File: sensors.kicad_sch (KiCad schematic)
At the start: 12 parts, among them U2 BMI088, U3 MMC5983MA, U4 MS5607-02BA

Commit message: rs232,can,ind,storage,usb v01
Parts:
- renumbered C34 to C27, C33 to C28, C25 to C29, C22 to C30, C21 to C31, C24 to C32, C23 to C33, C35 to C34, C20 to C35, U3 to U2, U2 to U3
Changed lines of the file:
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@@
 		(dnp no)
 		(fields_autoplaced yes)
-		(property "Reference" "#PWR013"
+		(property "Reference" "#PWR023"
 			(at 52.07 68.58 0)
 			(effects
@@
 			(project "hoppen_fc"
 				(path "/abe950a1-9eef-4508-9fd4-31d3e723e029/c85454e5-a89e-41eb-a5ed-71b4fc4cf13a/328607b5-eaf8-4cbb-82fe-138ea1b53a88"
-					(reference "#PWR013")
+					(reference "#PWR023")
 					(unit 1)
 				)
@@
 		(dnp no)
 		(fields_autoplaced yes)
-		(property "Reference" "#PWR012"
+		(property "Reference" "#PWR027"
 			(at 96.52 68.58 0)
 			(effects
@@
 			(project "hoppen_fc"
 				(path "/abe950a1-9eef-4508-9fd4-31d3e723e029/c85454e5-a89e-41eb-a5ed-71b4fc4cf13a/328607b5-eaf8-4cbb-82fe-138ea1b53a88"
-					(reference "#PWR012")
+					(reference "#PWR027")
 					(unit 1)
 				)
@@
 		(dnp no)
 		(fields_autoplaced yes)
-		(property "Reference" "#PWR019"
+		(property "Reference" "#PWR025"
 			(at 85.09 187.96 0)
 			(effects
@@
 			(project "hoppen_fc"
 				(path "/abe950a1-9eef-4508-9fd4-31d3e723e029/c85454e5-a89e-41eb-a5ed-71b4fc4cf13a/328607b5-eaf8-4cbb-82fe-138ea1b53a88"
-					(reference "#PWR019")
+					(reference "#PWR025")
 					(unit 1)
 				)
@@
 		(dnp no)
 		(fields_autoplaced yes)
-		(property "Reference" "#PWR017"
+		(property "Reference" "#PWR028"
 			(at 96.52 114.3 0)
 			(effects
@@
 			(project "hoppen_fc"
 				(path "/abe950a1-9eef-4508-9fd4-31d3e723e029/c85454e5-a89e-41eb-a5ed-71b4fc4cf13a/328607b5-eaf8-4cbb-82fe-138ea1b53a88"
-					(reference "#PWR017")
+					(reference "#PWR028")
 					(unit 1)
 				)
@@
 		(dnp no)
 		(fields_autoplaced yes)
-		(property "Reference" "#PWR020"
+		(property "Reference" "#PWR030"
 			(at 99.06 154.94 0)
 			(effects
@@
 			(project "hoppen_fc"
 				(path "/abe950a1-9eef-4508-9fd4-31d3e723e029/c85454e5-a89e-41eb-a5ed-71b4fc4cf13a/328607b5-eaf8-4cbb-82fe-138ea1b53a88"
-					(reference "#PWR020")
+					(reference "#PWR030")
 					(unit 1)
 				)
@@
 		(dnp no)
 		(fields_autoplaced yes)
-		(property "Reference" "C34"
+		(property "Reference" "C27"
 			(at 46.99 143.5099 0)
 			(effects
@@
 			(project "hoppen_fc"
 				(path "/abe950a1-9eef-4508-9fd4-31d3e723e029/c85454e5-a89e-41eb-a5ed-71b4fc4cf13a/328607b5-eaf8-4cbb-82fe-138ea1b53a88"
-					(reference "C34")
+					(reference "C27")
 					(unit 1)
 				)
@@
 		(dnp no)
 		(fields_autoplaced yes)
-		(property "Reference" "C23"
+		(property "Reference" "C33"
 			(at 102.87 172.7199 0)
 			(effects
@@
 			(project "hoppen_fc"
 				(path "/abe950a1-9eef-4508-9fd4-31d3e723e029/c85454e5-a89e-41eb-a5ed-71b4fc4cf13a/328607b5-eaf8-4cbb-82fe-138ea1b53a88"
-					(reference "C23")
+					(reference "C33")
 					(unit 1)
 				)
@@
 		(dnp no)
 		(fields_autoplaced yes)
-		(property "Reference" "#PWR010"
+		(property "Reference" "#PWR033"
 			(at 185.42 82.55 0)
 			(effects
@@
 			(project ""
 				(path "/abe950a1-9eef-4508-9fd4-31d3e723e029/c85454e5-a89e-41eb-a5ed-71b4fc4cf13a/328607b5-eaf8-4cbb-82fe-138ea1b53a88"
-					(reference "#PWR010")
+					(reference "#PWR033")
 					(unit 1)
 				)
@@
 		(dnp no)
 		(fields_autoplaced yes)
-		(property "Reference" "#PWR022"
+		(property "Reference" "#PWR020"
 			(at 43.18 139.7 0)
 			(effects
@@
 			(project "hoppen_fc"
 				(path "/abe950a1-9eef-4508-9fd4-31d3e723e029/c85454e5-a89e-41eb-a5ed-71b4fc4cf13a/328607b5-eaf8-4cbb-82fe-138ea1b53a88"
-					(reference "#PWR022")
+					(reference "#PWR020")
 					(unit 1)
 				)
@@
 		(dnp no)
 		(fields_autoplaced yes)
-		(property "Reference" "C20"
+		(property "Reference" "C35"
 			(at 200.66 67.3099 0)
 			(effects
@@
 			(project "hoppen_fc"
 				(path "/abe950a1-9eef-4508-9fd4-31d3e723e029/c85454e5-a89e-41eb-a5ed-71b4fc4cf13a/328607b5-eaf8-4cbb-82fe-138ea1b53a88"
-					(reference "C20")
+					(reference "C35")
 					(unit 1)
 				)
@@
 		(dnp no)
 		(fields_autoplaced yes)
-		(property "Reference" "C25"
+		(property "Reference" "C29"
 			(at 59.69 143.5099 0)
 			(effects
@@
 			(project "hoppen_fc"
 				(path "/abe950a1-9eef-4508-9fd4-31d3e723e029/c85454e5-a89e-41eb-a5ed-71b4fc4cf13a/328607b5-eaf8-4cbb-82fe-138ea1b53a88"
-					(reference "C25")
+					(reference "C29")
 					(unit 1)
 				)
@@
 		(dnp no)
 		(fields_autoplaced yes)
-		(property "Reference" "U2"
+		(property "Reference" "U3"
 			(at 84.6933 59.69 0)
 			(effects
@@
 			(project ""
 				(path "/abe950a1-9eef-4508-9fd4-31d3e723e029/c85454e5-a89e-41eb-a5ed-71b4fc4cf13a/328607b5-eaf8-4cbb-82fe-138ea1b53a88"
-					(reference "U2")
+					(reference "U3")
 					(unit 1)
 				)
@@
 		(dnp no)
 		(fields_autoplaced yes)
-		(property "Reference" "C22"
+		(property "Reference" "C30"
 			(at 67.31 54.6099 0)
 			(effects
@@
 			(project "hoppen_fc"
 				(path "/abe950a1-9eef-4508-9fd4-31d3e723e029/c85454e5-a89e-41eb-a5ed-71b4fc4cf13a/328607b5-eaf8-4cbb-82fe-138ea1b53a88"
-					(reference "C22")
+					(reference "C30")
 					(unit 1)
 				)
@@
 		(dnp no)
 		(fields_autoplaced yes)
-		(property "Reference" "#PWR018"
+		(property "Reference" "#PWR031"
 			(at 99.06 187.96 0)
 			(effects
@@
 			(project "hoppen_fc"
 				(path "/abe950a1-9eef-4508-9fd4-31d3e723e029/c85454e5-a89e-41eb-a5ed-71b4fc4cf13a/328607b5-eaf8-4cbb-82fe-138ea1b53a88"
-					(reference "#PWR018")
+					(reference "#PWR031")
 					(unit 1)
 				)
@@
 		(dnp no)
 		(fields_autoplaced yes)
-		(property "Reference" "C33"
+		(property "Reference" "C28"
 			(at 55.88 54.6099 0)
 			(effects
@@
 			(project "hoppen_fc"
 				(path "/abe950a1-9eef-4508-9fd4-31d3e723e029/c85454e5-a89e-41eb-a5ed-71b4fc4cf13a/328607b5-eaf8-4cbb-82fe-138ea1b53a88"
-					(reference "C33")
+					(reference "C28")
 					(unit 1)
 				)
@@
 		(dnp no)
 		(fields_autoplaced yes)
-		(property "Reference" "C35"
+		(property "Reference" "C34"
 			(at 189.23 67.3099 0)
 			(effects
@@
 			(project "hoppen_fc"
 				(path "/abe950a1-9eef-4508-9fd4-31d3e723e029/c85454e5-a89e-41eb-a5ed-71b4fc4cf13a/328607b5-eaf8-4cbb-82fe-138ea1b53a88"
-					(reference "C35")
+					(reference "C34")
 					(unit 1)
 				)
@@
 		(dnp no)
 		(fields_autoplaced yes)
-		(property "Reference" "#PWR014"
+		(property "Reference" "#PWR026"
 			(at 96.52 50.8 0)
 			(effects
@@
 			(project "hoppen_fc"
 				(path "/abe950a1-9eef-4508-9fd4-31d3e723e029/c85454e5-a89e-41eb-a5ed-71b4fc4cf13a/328607b5-eaf8-4cbb-82fe-138ea1b53a88"
-					(reference "#PWR014")
+					(reference "#PWR026")
 					(unit 1)
 				)
@@
 		(on_board yes)
 		(dnp no)
-		(property "Reference" "U3"
+		(property "Reference" "U2"
 			(at 66.04 147.32 0)
 			(effects
@@
 			(project ""
 				(path "/abe950a1-9eef-4508-9fd4-31d3e723e029/c85454e5-a89e-41eb-a5ed-71b4fc4cf13a/328607b5-eaf8-4cbb-82fe-138ea1b53a88"
-					(reference "U3")
+					(reference "U2")
 					(unit 1)
 				)
@@
 		(dnp no)
 		(fields_autoplaced yes)
-		(property "Reference" "#PWR015"
+		(property "Reference" "#PWR022"
 			(at 52.07 50.8 0)
 			(effects
@@
 			(project "hoppen_fc"
 				(path "/abe950a1-9eef-4508-9fd4-31d3e723e029/c85454e5-a89e-41eb-a5ed-71b4fc4cf13a/328607b5-eaf8-4cbb-82fe-138ea1b53a88"
-					(reference "#PWR015")
+					(reference "#PWR022")
 					(unit 1)
 				)
@@
 		(dnp no)
 		(fields_autoplaced yes)
-		(property "Reference" "C21"
+		(property "Reference" "C31"
 			(at 100.33 54.6099 0)
 			(effects
@@
 			(project "hoppen_fc"
 				(path "/abe950a1-9eef-4508-9fd4-31d3e723e029/c85454e5-a89e-41eb-a5ed-71b4fc4cf13a/328607b5-eaf8-4cbb-82fe-138ea1b53a88"
-					(reference "C21")
+					(reference "C31")
 					(unit 1)
 				)
@@
 		(dnp no)
 		(fields_autoplaced yes)
-		(property "Reference" "#PWR016"
+		(property "Reference" "#PWR024"
 			(at 82.55 114.3 0)
 			(effects
@@
 			(project "hoppen_fc"
 				(path "/abe950a1-9eef-4508-9fd4-31d3e723e029/c85454e5-a89e-41eb-a5ed-71b4fc4cf13a/328607b5-eaf8-4cbb-82fe-138ea1b53a88"
-					(reference "#PWR016")
+					(reference "#PWR024")
 					(unit 1)
 				)
@@
 		(dnp no)
 		(fields_autoplaced yes)
-		(property "Reference" "#PWR023"
+		(property "Reference" "#PWR029"
 			(at 99.06 139.7 0)
 			(effects
@@
 			(project "hoppen_fc"
 				(path "/abe950a1-9eef-4508-9fd4-31d3e723e029/c85454e5-a89e-41eb-a5ed-71b4fc4cf13a/328607b5-eaf8-4cbb-82fe-138ea1b53a88"
-					(reference "#PWR023")
+					(reference "#PWR029")
 					(unit 1)
 				)
@@
 		(dnp no)
 		(fields_autoplaced yes)
-		(property "Reference" "#PWR011"
+		(property "Reference" "#PWR032"
 			(at 185.42 64.77 0)
 			(effects
@@
 			(project ""
 				(path "/abe950a1-9eef-4508-9fd4-31d3e723e029/c85454e5-a89e-41eb-a5ed-71b4fc4cf13a/328607b5-eaf8-4cbb-82fe-138ea1b53a88"
-					(reference "#PWR011")
+					(reference "#PWR032")
 					(unit 1)
 				)
@@
 		(dnp no)
 		(fields_autoplaced yes)
-		(property "Reference" "C24"
+		(property "Reference" "C32"
 			(at 102.87 143.5099 0)
 			(effects
@@
 			(project "hoppen_fc"
 				(path "/abe950a1-9eef-4508-9fd4-31d3e723e029/c85454e5-a89e-41eb-a5ed-71b4fc4cf13a/328607b5-eaf8-4cbb-82fe-138ea1b53a88"
-					(reference "C24")
-					(unit 1)
-				)
+					(reference "C32")
+					(unit 1)
+				)

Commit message: wen branch and pr
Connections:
- net IMU_MISO: now reaches U3.10 (SDO2), U3.15 (SDO1)
- net IMU_SCK: now reaches U3.8 (SCK/SCL)
- net IMU_MOSI: now reaches U3.9 (SDI/SDA)
- net MAG_SCK: now reaches U2.1 (SCL/SCK)
- net MAG_MOSI: now reaches U2.16 (SDA/MOSI)
- net MAG_MISO: now reaches U2.5 (MISO)
- net BARO_MISO: now reaches U4.6 (SDO/MISO)
- net BARO_MOSI: now reaches U4.7 (SDI/MOSI)
- net BARO_SCK: now reaches U4.8 (CLK)
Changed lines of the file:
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@@
+		)
+	)
+	(text_box "SOFTWARE IMPLEMENTATION NOTE:\n8 bits\nMSB first\nMode 0 (CPOL=CPHA=0)\n\nBMI088 put on its own bus due to availability"
+		(exclude_from_sim no)
+		(at 177.8 127 0)
+		(size 63.5 25.4)
+		(margins 0.9525 0.9525 0.9525 0.9525)
+		(stroke
+			(width 0.4572)
+			(type solid)
+			(color 255 0 255 1)
+		)
+		(fill
+			(type none)
+		)
+		(effects
+			(font
+				(face "KiCad Font")
+				(size 1.524 1.524)
+			)
+			(justify left top)
 		)
 	)
@@
 	)
 	(bus_entry
-		(at 54.61 163.83)
+		(at 48.26 163.83)
 		(size 2.54 2.54)
 		(stroke
@@
 	)
 	(bus_entry
-		(at 54.61 158.75)
+		(at 48.26 158.75)
 		(size 2.54 2.54)
 		(stroke
@@
 	)
 	(bus_entry
-		(at 54.61 161.29)
+		(at 48.26 161.29)
 		(size 2.54 2.54)
 		(stroke
@@
 	(bus
 		(pts
-			(xy 54.61 163.83) (xy 54.61 161.29)
+			(xy 48.26 163.83) (xy 48.26 161.29)
 		)
 		(stroke
@@
 	(wire
 		(pts
-			(xy 57.15 166.37) (xy 62.23 166.37)
+			(xy 50.8 166.37) (xy 62.23 166.37)
 		)
 		(stroke
@@
 	(bus
 		(pts
-			(xy 54.61 161.29) (xy 54.61 158.75)
+			(xy 48.26 161.29) (xy 48.26 158.75)
 		)
 		(stroke
@@
 	(wire
 		(pts
-			(xy 57.15 161.29) (xy 62.23 161.29)
+			(xy 50.8 161.29) (xy 62.23 161.29)
 		)
 		(stroke
@@
 	(wire
 		(pts
-			(xy 57.15 163.83) (xy 62.23 163.83)
+			(xy 50.8 163.83) (xy 62.23 163.83)
 		)
 		(stroke
@@
 	(bus
 		(pts
-			(xy 54.61 158.75) (xy 50.8 158.75)
+			(xy 48.26 158.75) (xy 44.45 158.75)
 		)
 		(stroke
@@
 			(width 0)
 			(type default)
+		)
+	)
+	(label "IMU_SCK"
+		(at 57.15 78.74 0)
+		(effects
+			(font
+				(size 1.27 1.27)
+			)
+			(justify left bottom)
+		)
+	)
+	(label "BARO_SCK"
+		(at 250.19 63.5 180)
+		(effects
+			(font
+				(size 1.27 1.27)
+			)
+			(justify right bottom)
+		)
+	)
+	(label "BARO_MOSI"
+		(at 250.19 66.04 180)
+		(effects
+			(font
+				(size 1.27 1.27)
+			)
+			(justify right bottom)
+		)
+	)
+	(label "IMU_MISO"
+		(at 57.15 83.82 0)
+		(effects
+			(font
+				(size 1.27 1.27)
+			)
+			(justify left bottom)
+		)
+	)
+	(label "MAG_SCK"
+		(at 52.07 161.29 0)
+		(effects
+			(font
+				(size 1.27 1.27)
+			)
+			(justify left bottom)
+		)
+	)
+	(label "MAG_MOSI"
+		(at 52.07 163.83 0)
+		(effects
+			(font
+				(size 1.27 1.27)
+			)
+			(justify left bottom)
+		)
+	)
+	(label "MAG_MISO"
+		(at 52.07 166.37 0)
+		(effects
+			(font
+				(size 1.27 1.27)
+			)
+			(justify left bottom)
+		)
+	)
+	(label "BARO_MISO"
+		(at 250.19 68.58 180)
+		(effects
+			(font
+				(size 1.27 1.27)
+			)
+			(justify right bottom)
+		)
+	)
+	(label "IMU_MOSI"
+		(at 57.15 81.28 0)
+		(effects
+			(font
+				(size 1.27 1.27)
+			)
+			(justify left bottom)
 		)
 	)
@@
 		)
 	)
-	(hierarchical_label "SPI4"
+	(hierarchical_label "{SPI5}"
 		(shape input)
 		(at 257.81 60.96 0)
@@
 		)
 	)
-	(hierarchical_label "SPI4"
+	(hierarchical_label "{SPI5}"
 		(shape input)
-		(at 50.8 158.75 180)
+		(at 44.45 158.75 180)
 		(effects
 			(font
@@
 		)
 	)
-	(hierarchical_label "SPI4"
+	(hierarchical_label "{SPI4}"
 		(shape input)
 		(at 48.26 76.2 180)

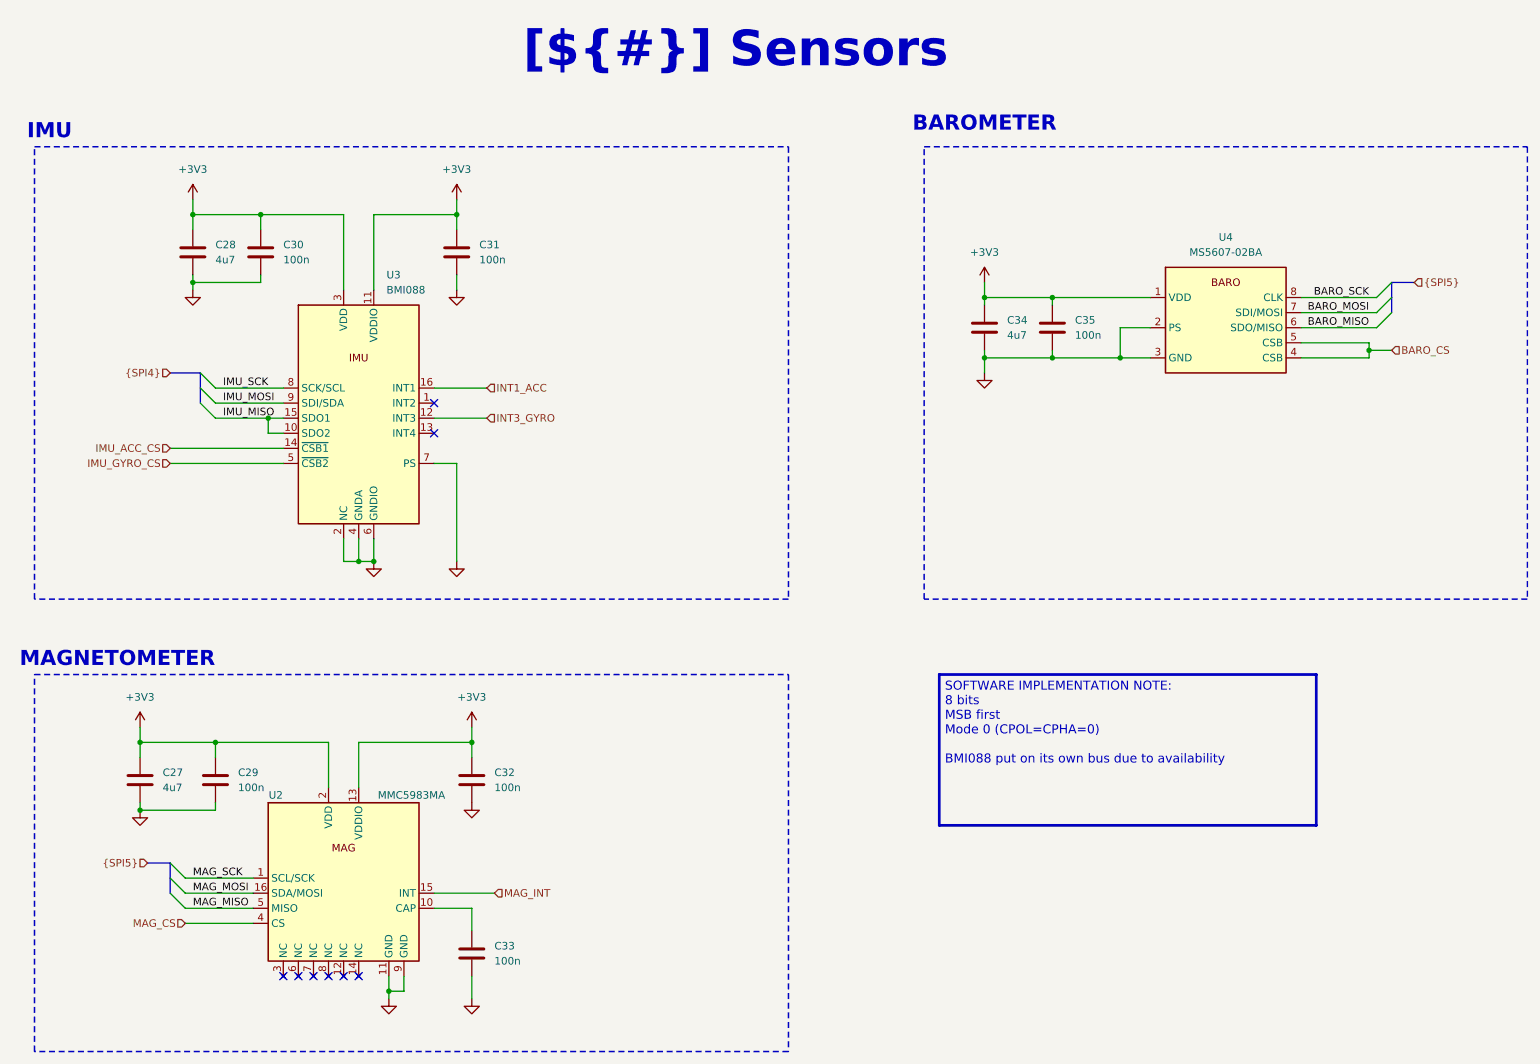
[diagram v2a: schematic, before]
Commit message: much work and .ioc file added
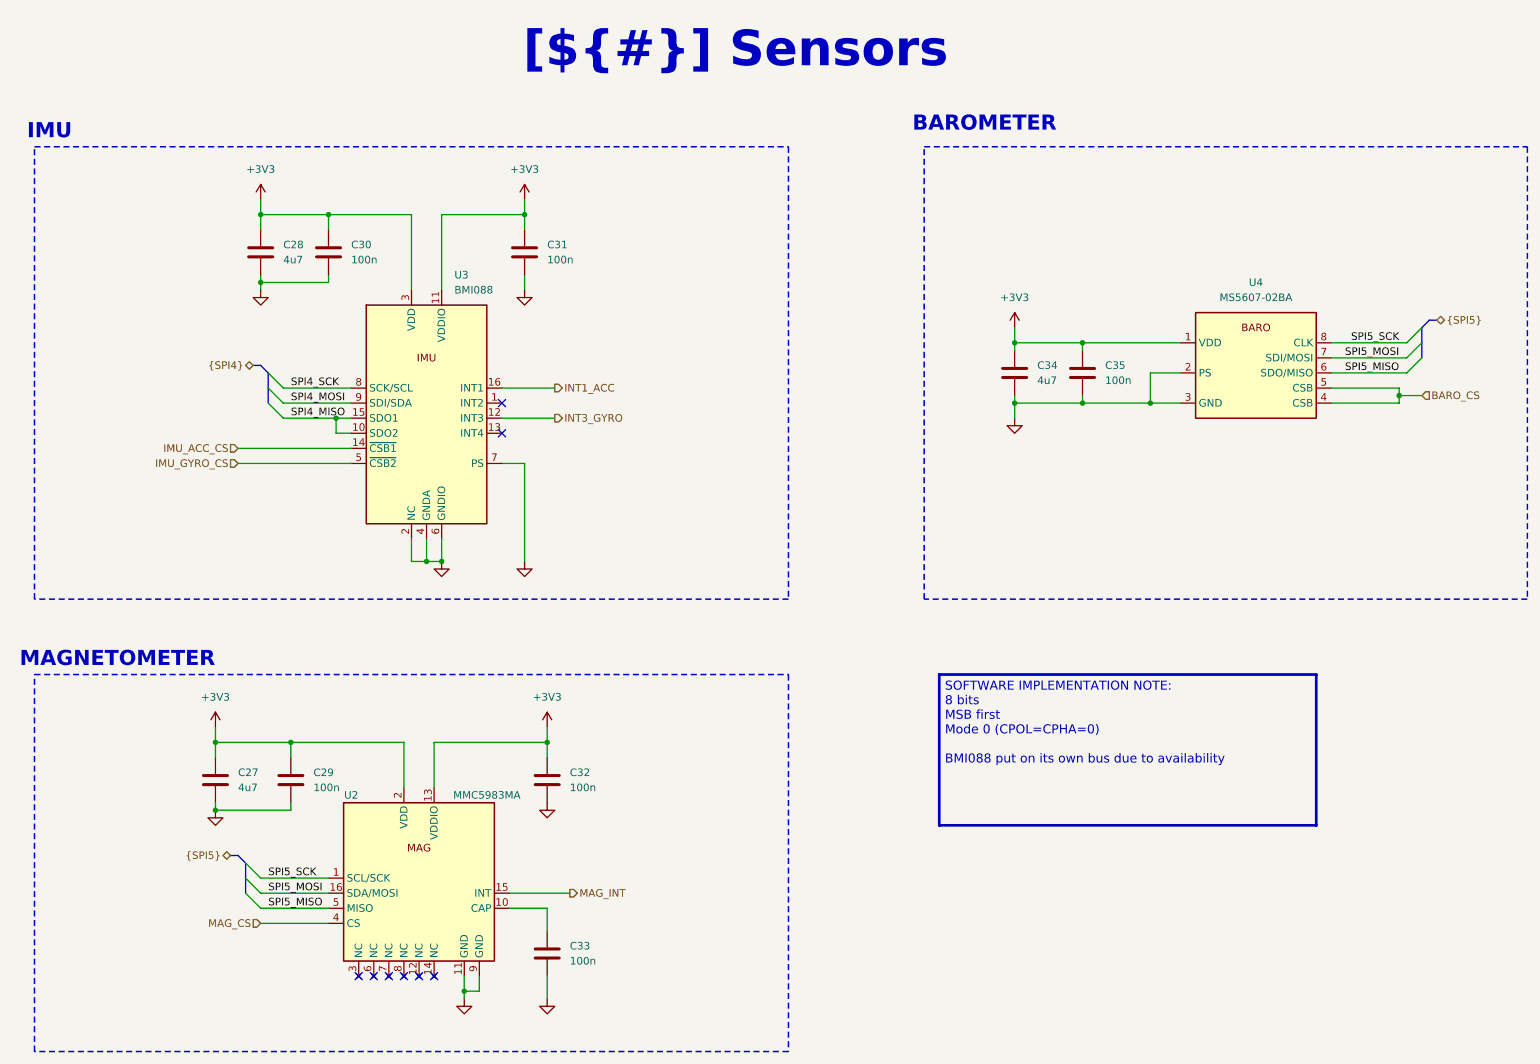
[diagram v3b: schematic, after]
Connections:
- net MAG_MISO is gone; now on net SPI5_MISO: U2.5 (MISO)
- net MAG_MOSI is gone; now on net SPI5_MOSI: U2.16 (SDA/MOSI)
- net MAG_SCK is gone; now on net SPI5_SCK: U2.1 (SCL/SCK)
- net BARO_MISO renamed SPI5_MISO
- net BARO_MOSI renamed SPI5_MOSI
- net BARO_SCK renamed SPI5_SCK
- net IMU_MISO renamed SPI4_MISO
- net IMU_MOSI renamed SPI4_MOSI
- net IMU_SCK renamed SPI4_SCK
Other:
- moved on the sheet: C27, C28, C29, C30, C31, C32, C33, C34, C35, U2, U3, U4
